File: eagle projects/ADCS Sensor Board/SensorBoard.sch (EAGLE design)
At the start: 95 parts, among them J5 HDR_10_EZFET_DEBUGGER, J6 MTI-1_8428-11B1-RK-TP, Q1 BC850SMD, Q2 IRF7507TRPBF, U1 MSP430F5529IPN, U2 LMV321, U3 ADS7841E_2K5, U4 LMV321, U5 LM20BIM7X_NOPB, U6 LMV321, Y1 32.768kHz, Y2 CSTCR4M00G15L99

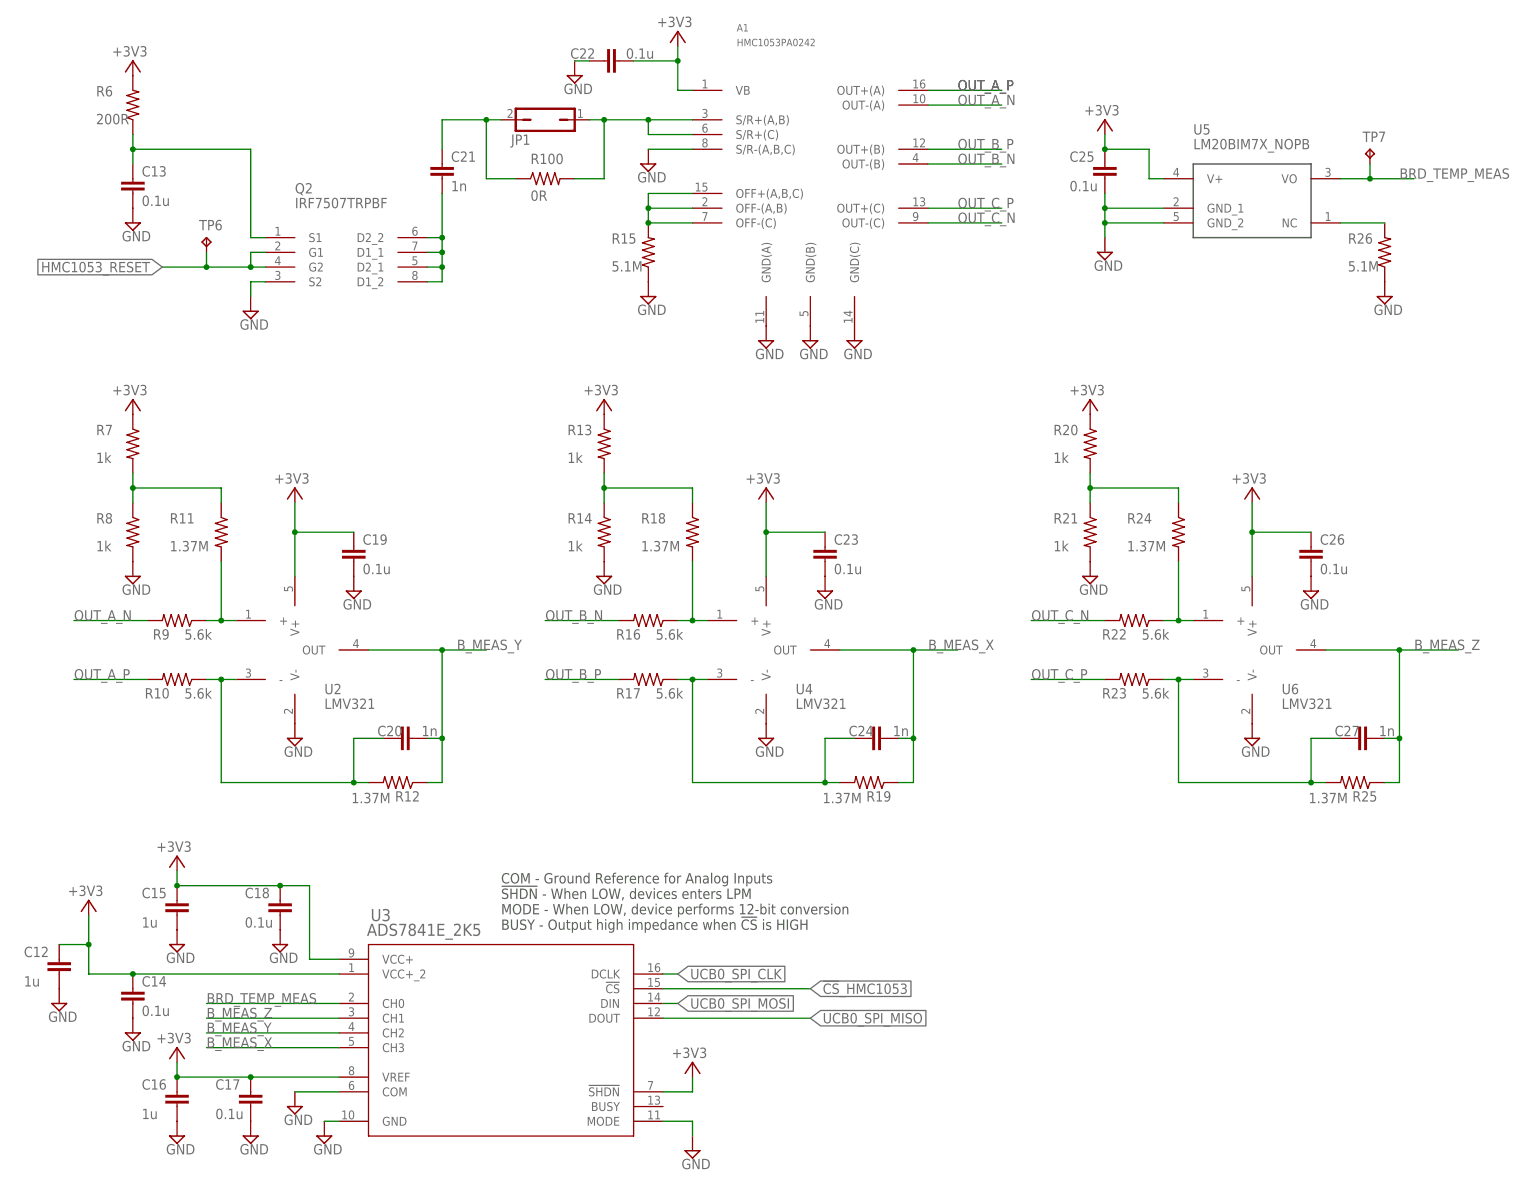
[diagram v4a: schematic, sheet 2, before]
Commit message: Removed temperature sensor
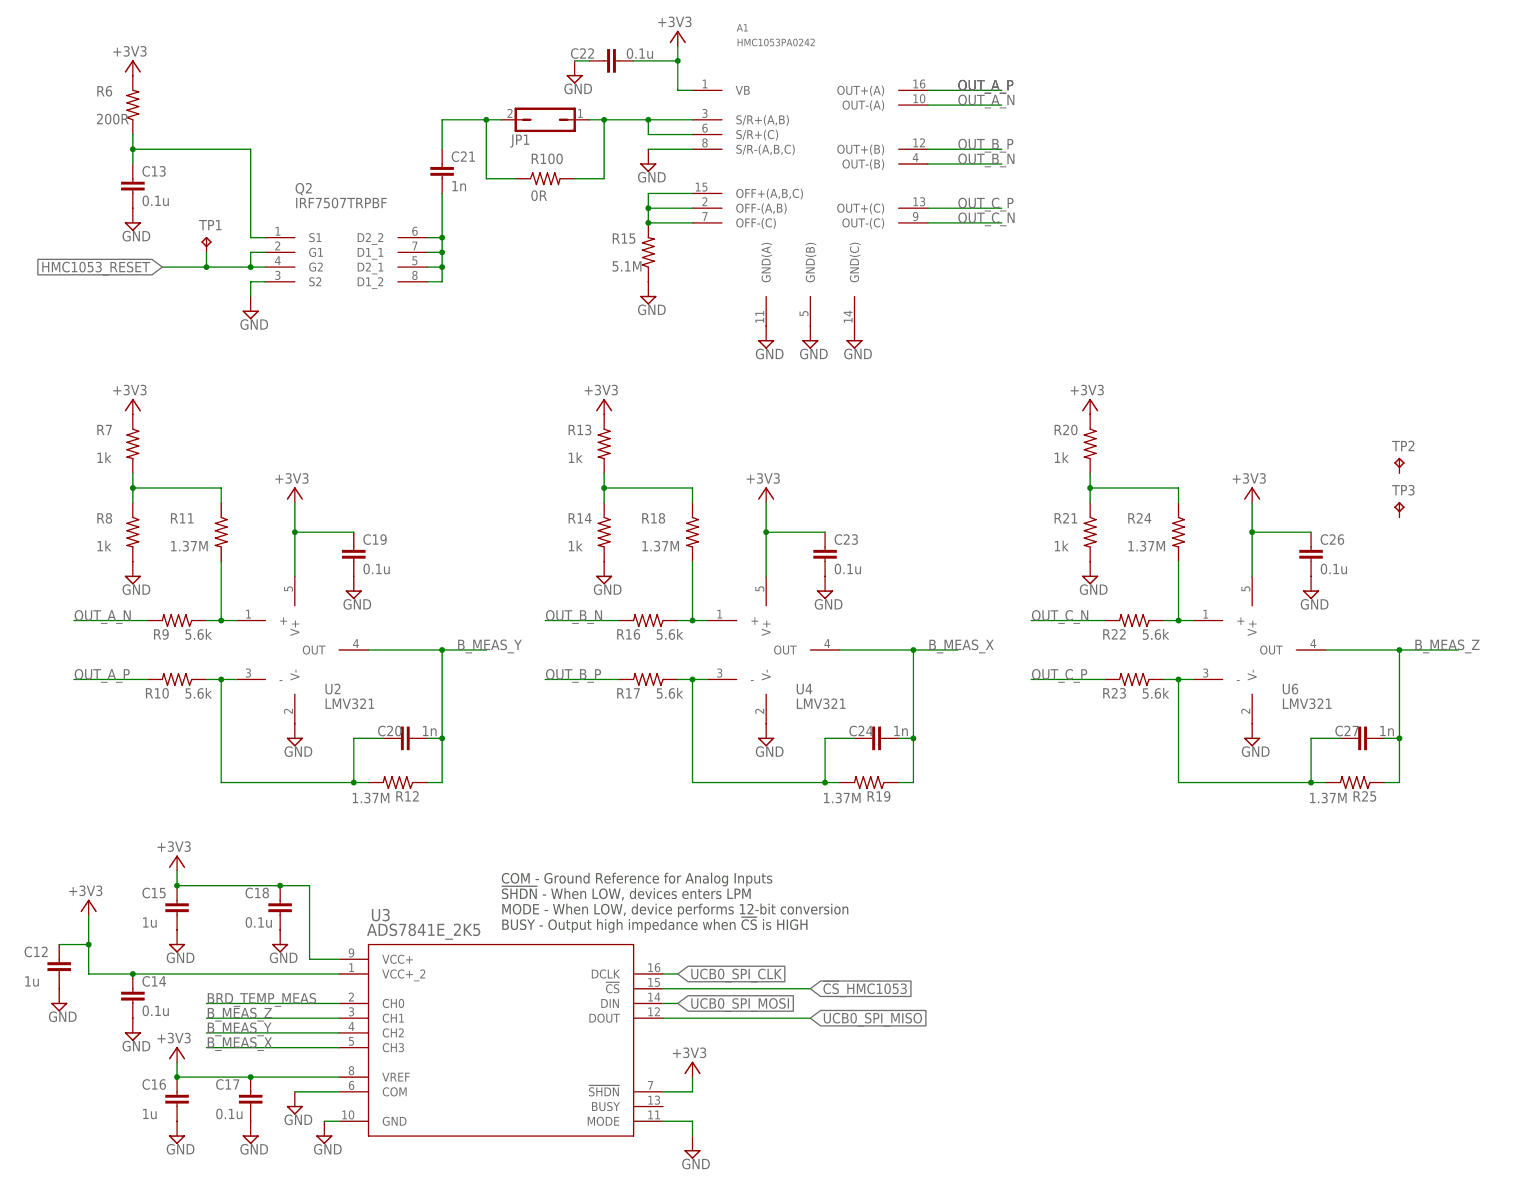
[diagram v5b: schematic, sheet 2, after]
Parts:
- removed C25: 0.1u, rcl:C-EUC0603
- removed R26: 5.1M, resistor:R-US_R1206
- removed TP6, TP7: TPB1,27, testpad:TPB1,27
- removed U5: LM20BIM7X_NOPB, my_library:LM20BIM7X_NOPB
- added TP1, TP2, TP3: TESTPOINT, my_library:TESTPOINT
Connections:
- removed net N$40: R26.2, U5.NC
- net +3V3: no longer C25.2, U5.V+
- net BRD_TEMP_MEAS: no longer TP7.TP, U5.VO
- net GND: no longer C25.1, R26.1, U5.GND_1, U5.GND_2
- net HMC1053_RESET: now also TP1.TP; no longer TP6.TP
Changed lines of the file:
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@@
 <part name="C13" library="rcl" library_urn="urn:adsk.eagle:library:334" deviceset="C-EU" device="C0603" package3d_urn="urn:adsk.eagle:package:23616/2" value="0.1u"/>
 <part name="SUPPLY55" library="supply2" library_urn="urn:adsk.eagle:library:372" deviceset="GND" device=""/>
-<part name="TP6" library="testpad" library_urn="urn:adsk.eagle:library:385" deviceset="TP" device="B1,27" package3d_urn="urn:adsk.eagle:package:27944/2" value="TPB1,27"/>
 <part name="Q2" library="my_library" library_urn="urn:adsk.eagle:library:22876504" deviceset="IRF7507TRPBF" device="" package3d_urn="urn:adsk.eagle:package:23087471/3"/>
 <part name="A1" library="my_library" library_urn="urn:adsk.eagle:library:22876504" deviceset="HMC1053" device="PA0242" package3d_urn="urn:adsk.eagle:package:24163034/3" value="HMC1053PA0242"/>
-<part name="U5" library="my_library" library_urn="urn:adsk.eagle:library:22876504" deviceset="LM20BIM7X_NOPB" device="" package3d_urn="urn:adsk.eagle:package:23087469/2"/>
-<part name="C25" library="rcl" library_urn="urn:adsk.eagle:library:334" deviceset="C-EU" device="C0603" package3d_urn="urn:adsk.eagle:package:23616/2" value="0.1u"/>
-<part name="SUPPLY56" library="supply2" library_urn="urn:adsk.eagle:library:372" deviceset="GND" device=""/>
-<part name="+3V25" library="supply1" library_urn="urn:adsk.eagle:library:371" deviceset="+3V3" device=""/>
-<part name="R26" library="resistor" library_urn="urn:adsk.eagle:library:348" deviceset="R-US_" device="R1206" package3d_urn="urn:adsk.eagle:package:23540/2" value="5.1M"/>
-<part name="SUPPLY57" library="supply2" library_urn="urn:adsk.eagle:library:372" deviceset="GND" device=""/>
-<part name="TP7" library="testpad" library_urn="urn:adsk.eagle:library:385" deviceset="TP" device="B1,27" package3d_urn="urn:adsk.eagle:package:27944/2" value="TPB1,27"/>
 <part name="U3" library="my_library" library_urn="urn:adsk.eagle:library:22876504" deviceset="ADS7841E_2K5" device="" package3d_urn="urn:adsk.eagle:package:23087509/3"/>
 <part name="C14" library="rcl" library_urn="urn:adsk.eagle:library:334" deviceset="C-EU" device="C0603" package3d_urn="urn:adsk.eagle:package:23616/2" value="0.1u"/>
@@
 <part name="+3V4" library="supply1" library_urn="urn:adsk.eagle:library:371" deviceset="+3V3" device=""/>
 <part name="P+2" library="supply1" library_urn="urn:adsk.eagle:library:371" deviceset="+5V" device=""/>
+<part name="TP1" library="my_library" library_urn="urn:adsk.eagle:library:22876504" deviceset="TESTPOINT" device="" package3d_urn="urn:adsk.eagle:package:24605432/1"/>
+<part name="TP2" library="my_library" library_urn="urn:adsk.eagle:library:22876504" deviceset="TESTPOINT" device="" package3d_urn="urn:adsk.eagle:package:24605432/1"/>
+<part name="TP3" library="my_library" library_urn="urn:adsk.eagle:library:22876504" deviceset="TESTPOINT" device="" package3d_urn="urn:adsk.eagle:package:24605432/1"/>
 </parts>
 <sheets>
@@
 <attribute name="VALUE" x="26.035" y="167.005" size="1.778" layer="96"/>
 </instance>
-<instance part="TP6" gate="G$1" x="40.64" y="167.64" smashed="yes">
-<attribute name="NAME" x="39.37" y="168.91" size="1.778" layer="95"/>
-<attribute name="TP_SIGNAL_NAME" x="41.91" y="166.37" size="1.778" layer="97"/>
-</instance>
 <instance part="Q2" gate="G$1" x="63.5" y="165.1" smashed="yes">
 <attribute name="VALUE" x="55.88" y="172.72" size="1.778" layer="96"/>
@@
 <attribute name="NAME" x="132.08" y="203.2" size="1.27" layer="95" font="vector" ratio="10"/>
 </instance>
-<instance part="U5" gate="G$1" x="220.98" y="175.26" smashed="yes">
-<attribute name="VALUE" x="210.82" y="182.88" size="1.778" layer="96"/>
-<attribute name="NAME" x="210.82" y="185.42" size="1.778" layer="95"/>
-</instance>
-<instance part="C25" gate="G$1" x="195.58" y="177.8" smashed="yes" rot="R180">
-<attribute name="NAME" x="189.484" y="180.721" size="1.778" layer="95"/>
-<attribute name="VALUE" x="189.484" y="175.641" size="1.778" layer="96"/>
-</instance>
-<instance part="SUPPLY56" gate="GND" x="195.58" y="165.1" smashed="yes">
-<attribute name="VALUE" x="193.675" y="161.925" size="1.778" layer="96"/>
-</instance>
-<instance part="+3V25" gate="G$1" x="195.58" y="187.96" smashed="yes">
-<attribute name="VALUE" x="198.12" y="190.5" size="1.778" layer="96" rot="R180"/>
-</instance>
-<instance part="R26" gate="G$1" x="243.84" y="165.1" smashed="yes" rot="R90">
-<attribute name="NAME" x="237.49" y="166.5986" size="1.778" layer="95"/>
-<attribute name="VALUE" x="237.49" y="161.798" size="1.778" layer="96"/>
-</instance>
-<instance part="SUPPLY57" gate="GND" x="243.84" y="157.48" smashed="yes">
-<attribute name="VALUE" x="241.935" y="154.305" size="1.778" layer="96"/>
-</instance>
-<instance part="TP7" gate="G$1" x="241.3" y="182.88" smashed="yes">
-<attribute name="NAME" x="240.03" y="184.15" size="1.778" layer="95"/>
-<attribute name="TP_SIGNAL_NAME" x="242.57" y="181.61" size="1.778" layer="97"/>
-</instance>
 <instance part="U3" gate="A" x="91.44" y="33.02" smashed="yes">
 <attribute name="NAME" x="68.9356" y="49.7586" size="2.0828" layer="95" ratio="6" rot="SR0"/>
@@
 <attribute name="VALUE" x="226.06" y="86.36" size="1.778" layer="96"/>
 <attribute name="NAME" x="226.06" y="88.9" size="1.778" layer="95"/>
+</instance>
+<instance part="TP1" gate="G$1" x="40.64" y="167.64" smashed="yes">
+<attribute name="NAME" x="39.37" y="168.91" size="1.778" layer="95"/>
+</instance>
+<instance part="TP2" gate="G$1" x="246.38" y="129.54" smashed="yes">
+<attribute name="NAME" x="245.11" y="130.81" size="1.778" layer="95"/>
+</instance>
+<instance part="TP3" gate="G$1" x="246.38" y="121.92" smashed="yes">
+<attribute name="NAME" x="245.11" y="123.19" size="1.778" layer="95"/>
 </instance>
 </instances>
@@
 <pinref part="R6" gate="G$1" pin="2"/>
 <pinref part="+3V24" gate="G$1" pin="+3V3"/>
-</segment>
-<segment>
-<pinref part="U5" gate="G$1" pin="V+"/>
-<wire x1="205.74" y1="177.8" x2="203.2" y2="177.8" width="0.1524" layer="91"/>
-<wire x1="203.2" y1="177.8" x2="203.2" y2="182.88" width="0.1524" layer="91"/>
-<wire x1="203.2" y1="182.88" x2="195.58" y2="182.88" width="0.1524" layer="91"/>
-<pinref part="+3V25" gate="G$1" pin="+3V3"/>
-<wire x1="195.58" y1="182.88" x2="195.58" y2="185.42" width="0.1524" layer="91"/>
-<pinref part="C25" gate="G$1" pin="2"/>
-<junction x="195.58" y="182.88"/>
 </segment>
 <segment>
@@
 <pinref part="SUPPLY50" gate="GND" pin="GND"/>
 <pinref part="A1" gate="G$1" pin="GND(C)"/>
-</segment>
-<segment>
-<pinref part="U5" gate="G$1" pin="GND_1"/>
-<wire x1="205.74" y1="172.72" x2="195.58" y2="172.72" width="0.1524" layer="91"/>
-<pinref part="C25" gate="G$1" pin="1"/>
-<wire x1="195.58" y1="172.72" x2="195.58" y2="175.26" width="0.1524" layer="91"/>
-<wire x1="195.58" y1="172.72" x2="195.58" y2="170.18" width="0.1524" layer="91"/>
-<junction x="195.58" y="172.72"/>
-<pinref part="U5" gate="G$1" pin="GND_2"/>
-<wire x1="205.74" y1="170.18" x2="195.58" y2="170.18" width="0.1524" layer="91"/>
-<pinref part="SUPPLY56" gate="GND" pin="GND"/>
-<wire x1="195.58" y1="167.64" x2="195.58" y2="170.18" width="0.1524" layer="91"/>
-<junction x="195.58" y="170.18"/>
-</segment>
-<segment>
-<pinref part="R26" gate="G$1" pin="1"/>
-<pinref part="SUPPLY57" gate="GND" pin="GND"/>
 </segment>
 <segment>
@@
 <wire x1="48.26" y1="162.56" x2="40.64" y2="162.56" width="0.1524" layer="91"/>
 <junction x="48.26" y="162.56"/>
-<pinref part="TP6" gate="G$1" pin="TP"/>
 <wire x1="40.64" y1="165.1" x2="40.64" y2="162.56" width="0.1524" layer="91"/>
 <junction x="40.64" y="162.56"/>
@@
 <pinref part="Q2" gate="G$1" pin="G2"/>
 <label x="33.02" y="162.56" size="1.778" layer="95" rot="R180" xref="yes"/>
+<pinref part="TP1" gate="G$1" pin="TP"/>
 </segment>
 </net>
@@
 <junction x="27.94" y="182.88"/>
 <pinref part="Q2" gate="G$1" pin="S1"/>
-</segment>
-</net>
-<net name="N$40" class="0">
-<segment>
-<pinref part="U5" gate="G$1" pin="NC"/>
-<pinref part="R26" gate="G$1" pin="2"/>
-<wire x1="236.22" y1="170.18" x2="243.84" y2="170.18" width="0.1524" layer="91"/>
 </segment>
 </net>
@@
 <net name="BRD_TEMP_MEAS" class="0">
 <segment>
-<pinref part="U5" gate="G$1" pin="VO"/>
-<wire x1="236.22" y1="177.8" x2="241.3" y2="177.8" width="0.1524" layer="91"/>
-<pinref part="TP7" gate="G$1" pin="TP"/>
-<wire x1="241.3" y1="177.8" x2="248.92" y2="177.8" width="0.1524" layer="91"/>
-<wire x1="241.3" y1="180.34" x2="241.3" y2="177.8" width="0.1524" layer="91"/>
-<junction x="241.3" y="177.8"/>
-<label x="246.38" y="177.8" size="1.778" layer="95"/>
-</segment>
-<segment>
 <wire x1="40.64" y1="35.56" x2="63.5" y2="35.56" width="0.1524" layer="91"/>

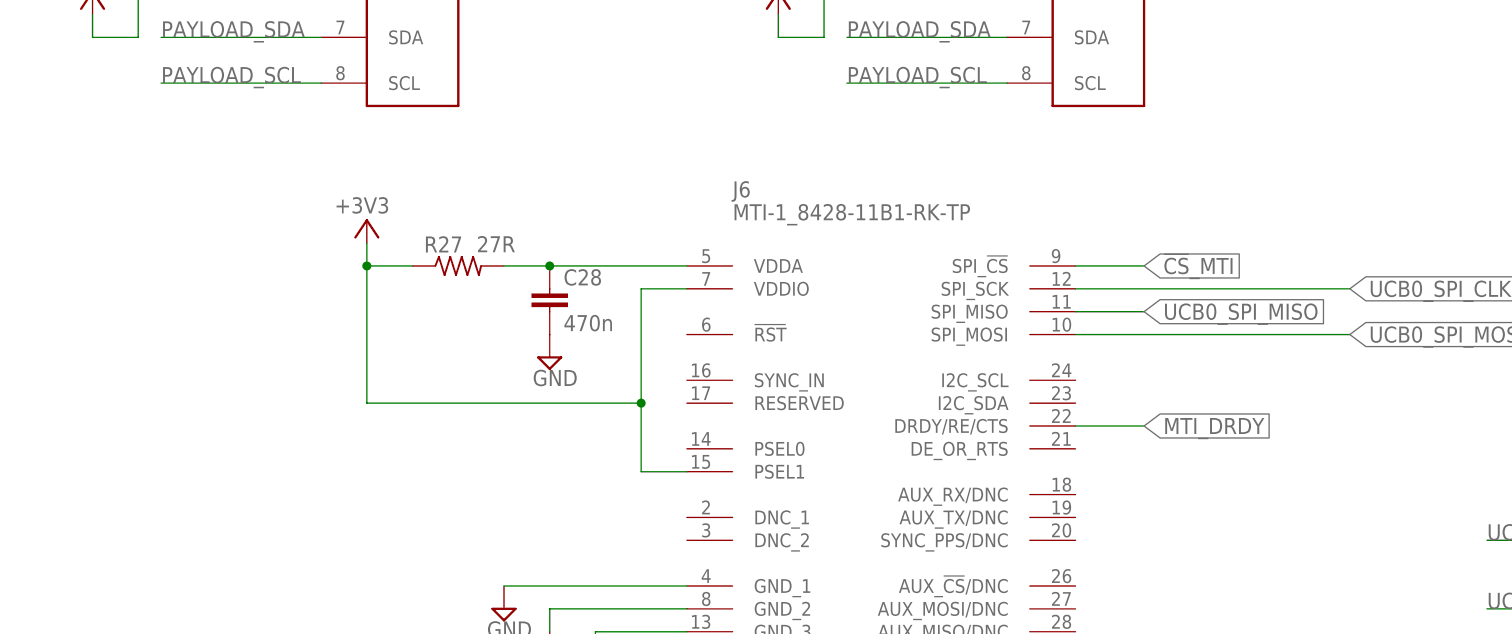
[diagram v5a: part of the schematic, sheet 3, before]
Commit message: Added testpoints, updated drill chart
Added missing MTI-1 IMU reset signal to msp430
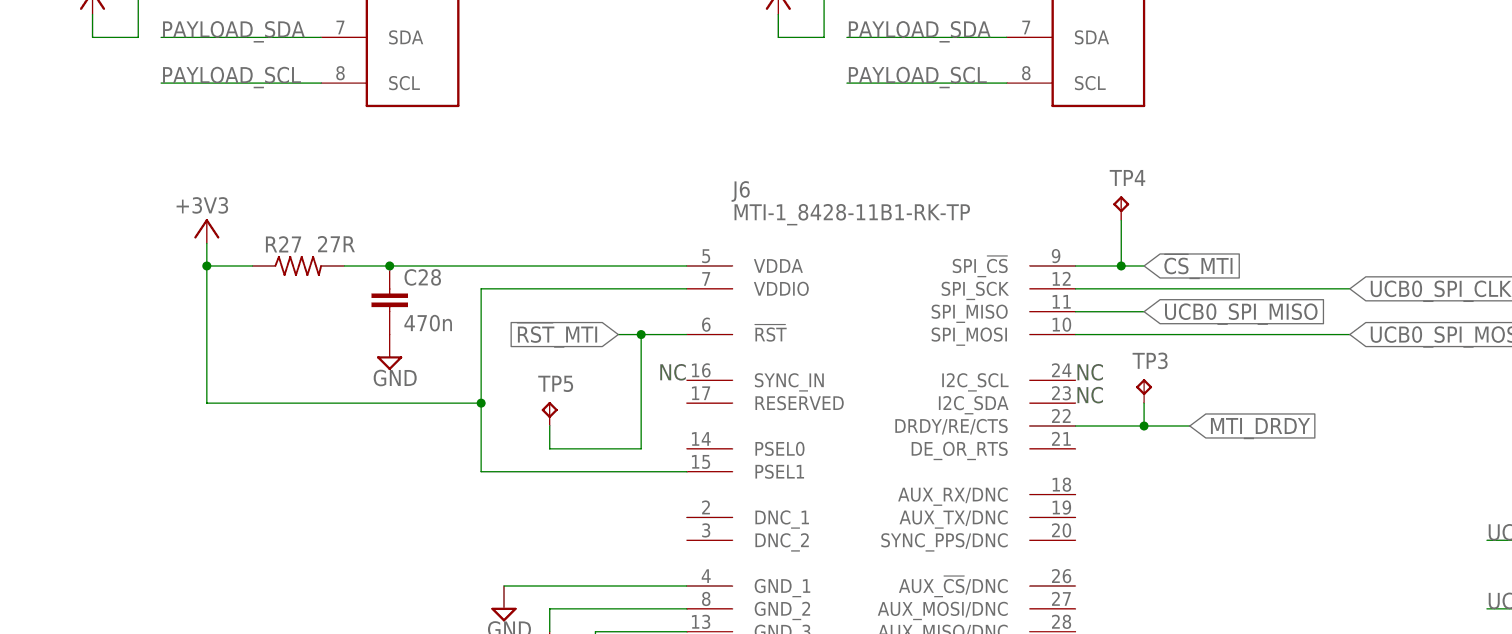
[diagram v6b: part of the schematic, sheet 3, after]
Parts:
- added TP4, TP5: TESTPOINT, my_library:TESTPOINT
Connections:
- removed net BRD_TEMP_MEAS: U3.CH0
- new net !RST!_MTI: J6.!RST, TP5.TP, U1.PU.1/DM
- net !CS!_HMC1053: now also TP2.TP
- net !CS!_MTI: now also TP4.TP
- net MTI_DRDY: now also TP3.TP
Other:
- moved on the sheet: C28, R27, R5, TP2
